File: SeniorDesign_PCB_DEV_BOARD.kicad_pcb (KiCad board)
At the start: 4 copper layers, 285.5 x 80.8 mm, 368 parts, among them J1 Conn_01x04_Pin, J10 Conn_01x02_Socket, J11 Conn_01x02_Pin, J12 USB_C_Receptacle_USB2.0_14P, J13 USB_C_Receptacle_USB2.0_14P, J14 IDC_Cable_02x08, J15 Conn_01x02_Pin, J16 Conn_01x04_Pin, J17 Conn_01x04_Pin, J18 Micro_SD_Card, J19 Conn_01x02_Socket, J2 Conn_01x02_Socket, J20 Conn_01x02_Socket, J21 MIC_I2S_CONNECTOR, J22 Conn_01x02_Socket, J23 Conn_01x02_Socket, J24 Conn_01x02_Socket, J3 Conn_01x03_Socket, J4 Conn_01x04_Pin, J5 Conn_01x02_Pin, J6 Conn_01x02_Socket, J7 Conn_01x02_Socket, J8 Conn_01x02_Socket, J9 Barrel_Jack, Q1 NMOS, Q2 NMOS, Q4 AO3400A, Q5 AO3400A, SW2 SW_Push, SW5 SW_Push, SW6 SW_Push, SW7 SW_Push, U1 TMP117xxDRV, U10 INA219AxD, U11 TLV62569ADRL, U12 USBLC6-2P6, U13 USBLC6-2P6, U14 ESP32-C3FH4, U15 TPS60400DBV, U16 TLV172IDCK, U2 RV-3028-C7, U3 STM32G474RETx, U5 MAX98357A, U6 TLV172IDCK, U7 TLV172IDCK, U8 MAX98357A, U9 INA219AxD, Y1 16MHz, Y2 40MHz

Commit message: taking a break
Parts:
- removed the AE1 at (236.9, 73.7)
- removed the C1 at (283.8, 90.4)
- removed the C10 at (293.2, 96.9)
- removed the C11 at (302.0, 96.3)
- removed the C12 at (250.1, 105.6)
- removed the C13 at (248.6, 105.6)
- removed the C14 at (301.7, 74.6)
- removed the C15 at (272.0, 75.3)
- removed the C16 at (255.2, 106.2)
- removed the C17 at (253.7, 106.2)
- removed the C18 at (317.2, 88.3)
- removed the C19 at (326.6, 91.1)
- removed the C2 at (283.9, 94.6)
- removed the C22 at (301.5, 107.5)
- removed the C23 at (240.6, 107.3)
- removed the C24 at (301.5, 105.7)
- removed the C25 at (240.6, 105.5)
- removed the C26 at (240.6, 87.3)
- removed the C27 at (240.6, 84.3)
- removed the C28 at (236.4, 74.7)
- removed the C29 at (236.4, 77.6)
- removed the C3 at (283.8, 92.5)
- removed the C30 at (236.4, 78.5)
- removed the C31 at (236.4, 81.5)
- removed the C32 at (236.7, 85.8)
- removed the C33 at (234.5, 83.1)
- removed the C34 at (236.7, 87.5)
- removed the C35 at (233.5, 85.6)
- removed the C36 at (229.5, 83.2)
- removed the C37 at (233.5, 88.0)
- removed the C38 at (227.9, 83.2)
- removed the C39 at (236.7, 89.2)
- removed the C4 at (283.9, 96.6)
- removed the C40 at (272.5, 86.3)
- removed the C41 at (253.7, 82.5)
- removed the C42 at (302.0, 86.3)
- removed the C43 at (284.3, 76.3)
- removed the C44 at (270.9, 79.5)
- removed the C45 at (229.6, 109.3)
- removed the C46 at (307.3, 77.1)
- removed the C47 at (281.7, 77.5)
- removed the C48 at (280.1, 77.5)
- removed the C49 at (281.7, 80.6)
- removed the C5 at (295.8, 88.8)
- removed the C50 at (280.1, 80.6)
- removed the C52 at (322.8, 69.8)
- removed the C53 at (275.1, 79.4)
- removed the C6 at (292.5, 86.6)
- removed the C7 at (286.1, 86.7)
- removed the C8 at (291.9, 83.8)
- removed the C9 at (288.8, 83.8)
- removed the D2 at (288.8, 103.8)
- removed the D4 at (322.5, 89.5)
- removed the D6 at (240.3, 102.3)
- removed the D7 at (301.3, 102.4)
- removed the D8 at (264.1, 73.6)
- removed the D9 at (234.4, 94.0)
- removed the F1 at (344.1, 77.4)
- removed the J1 at (310.1, 70.5)
- removed the J10 at (333.1, 104.1)
- removed J11: Conn_01x02_Pin, Connector_PinHeader_2.54mm:PinHeader_1x02_P2.54mm_Vertical
- removed the J12 at (298.3, 112.0)
- removed the J13 at (237.5, 111.8)
- removed the J14 at (286.1, 109.3)
- removed the J15 at (267.7, 70.5)
- removed the J16 at (221.1, 103.7)
- removed the J17 at (221.0, 83.7)
- removed the J18 at (254.5, 74.8)
- removed the J19 at (329.4, 111.4)
- removed the J2 at (285.0, 70.5)
- removed the J20 at (320.8, 111.4)
- removed the J21 at (337.5, 70.5)
- removed J22, J23: Conn_01x02_Socket, Connector_PinHeader_2.54mm:PinHeader_1x02_P2.54mm_Vertical
- removed J24: Conn_01x02_Socket, Connector_Phoenix_SPT:PhoenixContact_SPT_2.5_2-H-5.0_1x02_P5.0mm_Horizontal
- removed the J3 at (296.1, 70.5)
- removed the J4 at (307.1, 111.4)
- removed the J5 at (318.8, 70.5)
- removed the J6 at (276.3, 70.5)
- removed the J7 at (246.6, 111.4)
- removed the J8 at (256.0, 111.4)
- removed the L2 at (236.9, 76.1)
- removed the L3 at (236.8, 80.0)
- removed the L4 at (232.0, 82.4)
- removed the Q1 at (324.6, 100.9)
- removed the Q2 at (265.9, 76.6)
- removed the Q4 at (318.9, 104.8)
- removed the Q5 at (314.9, 104.9)
- removed the R10 at (291.1, 95.8)
- removed the R11 at (288.1, 101.6)
- removed the R12 at (273.0, 96.4)
- removed the R13 at (273.0, 93.6)
- removed the R14 at (273.0, 91.1)
- removed the R17 at (302.0, 89.9)
- removed the R18 at (299.1, 83.1)
- removed the R19 at (302.0, 93.1)
- removed the R2 at (298.9, 78.7)
- removed the R20 at (247.1, 102.5)
- removed the R21 at (274.5, 74.6)
- removed the R22 at (270.2, 76.7)
- removed the R23 at (267.6, 79.7)
- removed the R24 at (276.5, 77.2)
- removed the R25 at (277.2, 79.7)
- removed the R26 at (274.5, 82.9)
- removed the R27 at (270.2, 83.1)
- removed the R28 at (269.7, 85.8)
- removed the R29 at (270.5, 88.1)
- removed the R3 at (284.2, 74.6)
- removed the R30 at (255.0, 102.7)
- removed the R31 at (329.0, 96.0)
- removed the R32 at (329.0, 99.1)
- removed the R33 at (324.9, 83.4)
- removed the R34 at (258.0, 102.7)
- removed the R35 at (250.1, 102.5)
- removed the R36 at (292.6, 74.6)
- removed the R37 at (302.0, 83.0)
- removed the R38 at (325.0, 93.2)
- removed the R39 at (321.5, 93.2)
- removed the R45 at (240.0, 112.5)
- removed the R46 at (295.8, 112.7)
- removed the R47 at (234.9, 112.4)
- removed the R48 at (297.5, 106.7)
- removed the R49 at (299.1, 106.7)
- removed the R5 at (288.6, 98.2)
- removed the R50 at (236.7, 106.6)
- removed the R51 at (238.2, 106.6)
- removed the R52 at (268.7, 77.4)
- removed the R53 at (268.7, 73.8)
- removed the R54 at (234.4, 91.0)
- removed the R55 at (228.6, 84.3)
- removed the R56 at (228.6, 86.0)
- removed the R57 at (232.7, 80.8)
- removed the R58 at (231.5, 90.9)
- removed the R59 at (228.6, 88.0)
- removed the R6 at (291.8, 92.9)
- removed the R60 at (232.7, 79.2)
- removed the R61 at (298.1, 113.8)
- removed the R62 at (237.5, 113.7)
- removed the R68 at (315.5, 83.3)
- removed the R69 at (317.6, 80.0)
- removed the R7 at (307.3, 78.7)
- removed the R70 at (313.9, 83.3)
- removed the R71 at (314.5, 80.0)
- removed the R72 at (324.1, 82.0)
- removed the R73 at (324.1, 80.4)
- removed the R74 at (321.0, 80.4)
- removed the R75 at (321.0, 82.0)
- removed the R76 at (229.6, 112.4)
- removed the R78 at (230.4, 114.8)
- removed the R79 at (229.4, 97.1)
- removed the R8 at (307.4, 75.6)
- removed the R80 at (319.8, 101.3)
- removed the R81 at (317.9, 101.2)
- removed the R82 at (327.4, 112.3)
- removed the R83 at (315.8, 101.3)
- removed the R84 at (313.9, 101.3)
- removed the R85 at (318.6, 112.2)
- removed the R9 at (289.3, 95.8)
- removed the SW2 at (304.6, 92.2)
- removed the SW5 at (304.7, 81.5)
- removed the SW6 at (227.2, 114.0)
- removed the SW7 at (230.2, 99.5)
- removed the U1 at (298.9, 78.7)
- removed the U10 at (323.8, 86.5)
- removed the U12 at (298.3, 103.6)
- removed the U13 at (237.5, 103.4)
- removed the U14 at (235.0, 86.3)
- removed the U15 at (284.5, 78.9)
- removed the U16 at (275.1, 79.6)
- removed the U2 at (307.4, 77.6)
- removed the U3 at (288.8, 92.5)
- removed the U5 at (248.8, 105.6)
- removed the U6 at (270.9, 79.8)
- removed the U7 at (272.5, 86.6)
- removed the U8 at (256.7, 105.6)
- removed the U9 at (320.0, 84.7)
- removed the Y1 at (290.3, 80.6)
- removed the Y2 at (243.7, 85.8)
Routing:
- net 3V3: track 277.3 -> 136.7 mm, vias 73 -> 36
- net /ESP32C3/SPI1_MISO: track 235.1 -> 122.9 mm, vias 8 -> 4
- net 5V: track 206.0 -> 98.9 mm, vias 18 -> 12
- net /Power/I2C3_SCL: track 216.6 -> 110.0 mm, vias 7 -> 3
- net /ESP32C3/SPI1_MOSI: track 197.9 -> 98.2 mm, vias 8 -> 4
- net USB_5V: track 214.7 -> 115.4 mm, vias 13 -> 6
- net /ESP32C3/SPI1_SCLK: track 193.6 -> 102.0 mm, vias 8 -> 4
- net /Power/I2C3_SDA: track 172.4 -> 94.3 mm, vias 5 -> 2
- net /ESP32C3/SPI1_CS_ESP: track 177.2 -> 105.4 mm, vias 4 -> 2
- net /STM32G4/I2S3_CK: track 101.2 -> 43.7 mm, vias 2 -> 1
- net /STM32G4/I2S3_WS: track 97.8 -> 42.7 mm, vias 2 -> 1
- net /Analog/LEFT_SD_MODE: track 110.2 -> 55.1 mm, vias 4 -> 2
- net /STM32G4/I2S3_SD: track 95.3 -> 41.0 mm, vias 2 -> 1
- net /ESP32C3/ESP32_RST: track 101.3 -> 50.6 mm
- net /STM32G4/nRST: track 102.1 -> 52.5 mm
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- removed copper zone on B.Cu, net (none)
- removed copper zone on F.Cu, net /Power/5V_AMPS_1
- removed copper zone on F.Cu, net Net-(J10-Pin_1)
- removed copper zone on F.Cu, net Net-(J24-Pin_2)
- removed copper zone on B.Cu, net USB_5V
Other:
- board size 285.5 x 80.8 mm -> 98.3 x 80.8 mm
- board text removed: "MASHED PCB"
- board text removed: "TEAM 20"
- board text removed: "V1 Rev0"

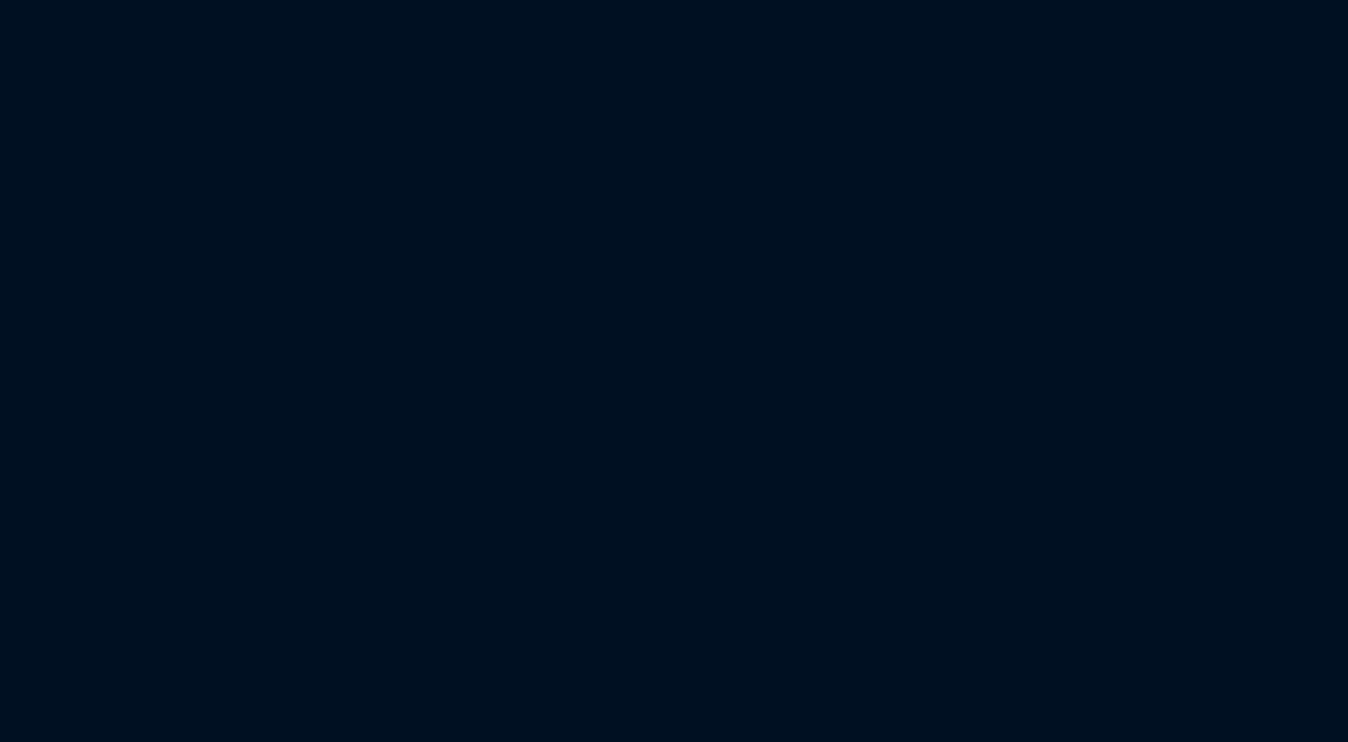
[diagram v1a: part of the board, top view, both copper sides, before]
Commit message: got rid of second buck
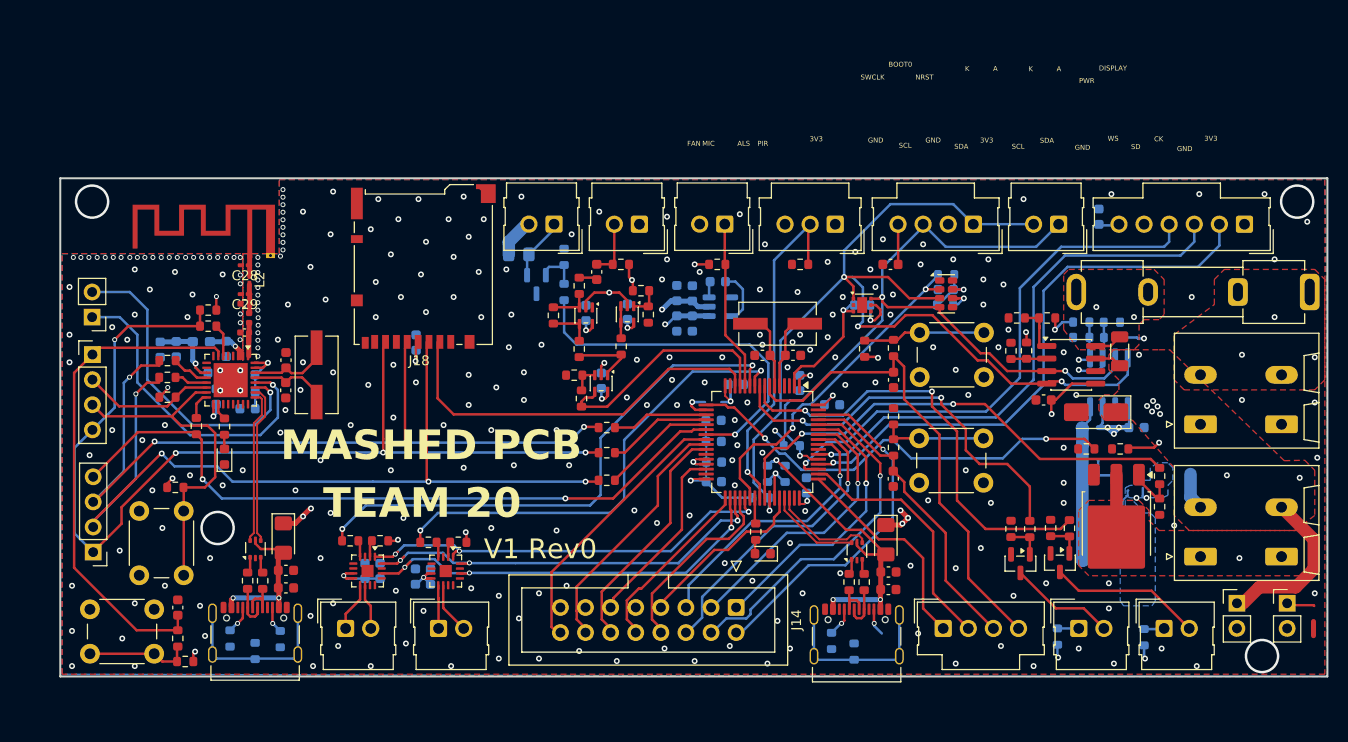
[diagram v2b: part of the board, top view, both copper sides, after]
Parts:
- added AE1: Antenna_Shield, RF_Antenna:Texas_SWRA117D_2.4GHz_Left, F.Cu at (236.9, 73.7)
- added C1: 1u, Capacitor_SMD:C_0603_1608Metric, B.Cu at (283.8, 90.4)
- added C10: 100n, Capacitor_SMD:C_0603_1608Metric, B.Cu at (293.2, 96.9)
- added C11: 100n, Capacitor_SMD:C_0603_1608Metric, F.Cu at (302.0, 96.3)
- added C12: 10u, Capacitor_SMD:C_0603_1608Metric, B.Cu at (250.1, 105.6)
- added C13: 100n, Capacitor_SMD:C_0603_1608Metric, B.Cu at (248.6, 105.6)
- added C14: 100n, Capacitor_SMD:C_0603_1608Metric, F.Cu at (301.7, 74.6)
- added C15: 1uF, Capacitor_SMD:C_0603_1608Metric, F.Cu at (272.0, 75.3)
- added C16: 10u, Capacitor_SMD:C_0603_1608Metric, B.Cu at (255.2, 106.2)
- added C17: 100n, Capacitor_SMD:C_0603_1608Metric, B.Cu at (253.7, 106.2)
- added C18: 100n, Capacitor_SMD:C_0603_1608Metric, F.Cu at (317.2, 88.3)
- added C19: 100n, Capacitor_SMD:C_0603_1608Metric, B.Cu at (326.6, 91.1)
- added C2: 100n, Capacitor_SMD:C_0603_1608Metric, B.Cu at (283.9, 94.6)
- added C22: 1u, Capacitor_SMD:C_0603_1608Metric, F.Cu at (301.5, 107.5)
- added C23: 1u, Capacitor_SMD:C_0603_1608Metric, F.Cu at (240.6, 107.3)
- added C24: 100n, Capacitor_SMD:C_0603_1608Metric, F.Cu at (301.5, 105.7)
- added C25: 100n, Capacitor_SMD:C_0603_1608Metric, F.Cu at (240.6, 105.5)
- added C26: 22p, Capacitor_SMD:C_0603_1608Metric, F.Cu at (240.6, 87.3)
- added C27: 22p, Capacitor_SMD:C_0603_1608Metric, F.Cu at (240.6, 84.3)
- added C28: DNP, Capacitor_SMD:C_0201_0603Metric_Pad0.64x0.40mm_HandSolder, F.Cu at (236.4, 74.7)
- added C29: DNP, Capacitor_SMD:C_0201_0603Metric_Pad0.64x0.40mm_HandSolder, F.Cu at (236.4, 77.6)
- added C3: 100n, Capacitor_SMD:C_0603_1608Metric, B.Cu at (283.8, 92.5)
- added C30: DNP, Capacitor_SMD:C_0402_1005Metric, F.Cu at (236.4, 78.5)
- added C31: DNP, Capacitor_SMD:C_0402_1005Metric, F.Cu at (236.4, 81.5)
- added C32: 100n, Capacitor_SMD:C_0603_1608Metric, B.Cu at (236.7, 85.8)
- added C33: 1u, Capacitor_SMD:C_0603_1608Metric, B.Cu at (234.5, 83.1)
- added C34: 100n, Capacitor_SMD:C_0603_1608Metric, B.Cu at (236.7, 87.5)
- added C35: 100n, Capacitor_SMD:C_0603_1608Metric, B.Cu at (233.5, 85.6)
- added C36: 100n, Capacitor_SMD:C_0603_1608Metric, B.Cu at (229.5, 83.2)
- added C37: 100n, Capacitor_SMD:C_0603_1608Metric, B.Cu at (233.5, 88.0)
- added C38: 10u, Capacitor_SMD:C_0603_1608Metric, B.Cu at (227.9, 83.2)
- added C39: 1u, Capacitor_SMD:C_0603_1608Metric, B.Cu at (236.7, 89.2)
- added C4: 100n, Capacitor_SMD:C_0603_1608Metric, B.Cu at (283.9, 96.6)
- added C40: 100n, Capacitor_SMD:C_0603_1608Metric, B.Cu at (272.5, 86.3)
- added C41: 100n, Capacitor_SMD:C_0603_1608Metric, B.Cu at (253.7, 82.5)
- added C42: 100n, Capacitor_SMD:C_0603_1608Metric, F.Cu at (302.0, 86.3)
- added C43: 1u, Capacitor_SMD:C_0603_1608Metric, B.Cu at (284.3, 76.3)
- added C44: 100n, Capacitor_SMD:C_0603_1608Metric, B.Cu at (270.9, 79.5)
- added C45: 100n, Capacitor_SMD:C_0603_1608Metric, F.Cu at (229.6, 109.3)
- added C46: 100n, Capacitor_SMD:C_0603_1608Metric, B.Cu at (307.3, 77.1)
- added C47: 100n, Capacitor_SMD:C_0603_1608Metric, B.Cu at (281.7, 77.5)
- added C48: 1u, Capacitor_SMD:C_0603_1608Metric, B.Cu at (280.1, 77.5)
- added C49: 1u, Capacitor_SMD:C_0603_1608Metric, B.Cu at (281.7, 80.6)
- added C5: 100n, Capacitor_SMD:C_0603_1608Metric, B.Cu at (295.8, 88.8)
- added C50: 100n, Capacitor_SMD:C_0603_1608Metric, B.Cu at (280.1, 80.6)
- added C52: 100n, Capacitor_SMD:C_0603_1608Metric, B.Cu at (322.8, 69.8)
- added C53: 100n, Capacitor_SMD:C_0603_1608Metric, B.Cu at (275.1, 79.4)
- added C6: 100n, Capacitor_SMD:C_0603_1608Metric, B.Cu at (292.5, 86.6)
- added C7: 100n, Capacitor_SMD:C_0603_1608Metric, B.Cu at (286.1, 86.7)
- added C8: 22p, Capacitor_SMD:C_0603_1608Metric, F.Cu at (291.9, 83.8)
- added C9: 22p, Capacitor_SMD:C_0603_1608Metric, F.Cu at (288.8, 83.8)
- added D2: LED, LED_SMD:LED_0603_1608Metric, F.Cu at (288.8, 103.8)
- added D4: SMAJ5.0A, Diode_SMD:D_SMA, F.Cu at (322.5, 89.5)
- added D6: D, Diode_SMD:D_1206_3216Metric_Pad1.42x1.75mm_HandSolder, F.Cu at (240.3, 102.3)
- added D7: D, Diode_SMD:D_1206_3216Metric_Pad1.42x1.75mm_HandSolder, F.Cu at (301.3, 102.4)
- added D8: D, Diode_SMD:D_0805_2012Metric_Pad1.15x1.40mm_HandSolder, B.Cu at (264.1, 73.6)
- added D9: LED, LED_SMD:LED_0603_1608Metric, F.Cu at (234.4, 94.0)
- added F1: RGEF1400, Fuse:Fuseholder_Clip-5x20mm_Keystone_3512P_Inline_P23.62x7.27mm_D1.02x2.41x1.02x1.57mm_Horizontal, F.Cu at (344.1, 77.4)
- added J1: Conn_01x04_Pin, Connector_Molex:Molex_SL_171971-0004_1x04_P2.54mm_Vertical, F.Cu at (310.1, 70.5)
- added J10: Conn_01x02_Socket, Connector_Phoenix_SPT:PhoenixContact_SPT_2.5_2-H-5.0_1x02_P5.0mm_Horizontal, F.Cu at (333.1, 104.1)
- added J11: Conn_01x02_Pin, Connector_PinHeader_2.54mm:PinHeader_1x02_P2.54mm_Vertical, F.Cu at (221.0, 79.9)
- added J12: USB_C_Receptacle_USB2.0_14P, Connector_USB:USB_C_Receptacle_Palconn_UTC16-G, F.Cu at (298.3, 112.0)
- added J13: USB_C_Receptacle_USB2.0_14P, Connector_USB:USB_C_Receptacle_Palconn_UTC16-G, F.Cu at (237.5, 111.8)
- added J14: IDC_Cable_02x08, Connector_IDC:IDC-Header_2x08_P2.54mm_Vertical, F.Cu at (286.1, 109.3)
- added J15: Conn_01x02_Pin, Connector_Molex:Molex_SL_171971-0002_1x02_P2.54mm_Vertical, F.Cu at (267.7, 70.5)
- added J16: Conn_01x04_Pin, Connector_PinHeader_2.54mm:PinHeader_1x04_P2.54mm_Vertical, F.Cu at (221.1, 103.7)
- added J17: Conn_01x04_Pin, Connector_PinHeader_2.54mm:PinHeader_1x04_P2.54mm_Vertical, F.Cu at (221.0, 83.7)
- added J18: Micro_SD_Card, Connector_Card:microSD_HC_Hirose_DM3BT-DSF-PEJS, F.Cu at (254.5, 74.8)
- added J19: Conn_01x02_Socket, Connector_Molex:Molex_SL_171971-0002_1x02_P2.54mm_Vertical, F.Cu at (329.4, 111.4)
- added J2: Conn_01x02_Socket, Connector_Molex:Molex_SL_171971-0002_1x02_P2.54mm_Vertical, F.Cu at (285.0, 70.5)
- added J20: Conn_01x02_Socket, Connector_Molex:Molex_SL_171971-0002_1x02_P2.54mm_Vertical, F.Cu at (320.8, 111.4)
- added J21: MIC_I2S_CONNECTOR, Connector_Molex:Molex_SL_171971-0006_1x06_P2.54mm_Vertical, F.Cu at (337.5, 70.5)
- added J22: Conn_01x02_Socket, Connector_PinHeader_2.54mm:PinHeader_1x02_P2.54mm_Vertical, F.Cu at (341.9, 108.9)
- added J23: Conn_01x02_Socket, Connector_PinHeader_2.54mm:PinHeader_1x02_P2.54mm_Vertical, F.Cu at (336.8, 108.9)
- added J24: Conn_01x02_Socket, Connector_Phoenix_SPT:PhoenixContact_SPT_2.5_2-H-5.0_1x02_P5.0mm_Horizontal, F.Cu at (333.1, 90.8)
- added J3: Conn_01x03_Socket, Connector_Molex:Molex_SL_171971-0003_1x03_P2.54mm_Vertical, F.Cu at (296.1, 70.5)
- added J4: Conn_01x04_Pin, Connector_Molex:Molex_SL_171971-0004_1x04_P2.54mm_Vertical, F.Cu at (307.1, 111.4)
- added J5: Conn_01x02_Pin, Connector_Molex:Molex_SL_171971-0002_1x02_P2.54mm_Vertical, F.Cu at (318.8, 70.5)
- added J6: Conn_01x02_Socket, Connector_Molex:Molex_SL_171971-0002_1x02_P2.54mm_Vertical, F.Cu at (276.3, 70.5)
- added J7: Conn_01x02_Socket, Connector_Molex:Molex_SL_171971-0002_1x02_P2.54mm_Vertical, F.Cu at (246.6, 111.4)
- added J8: Conn_01x02_Socket, Connector_Molex:Molex_SL_171971-0002_1x02_P2.54mm_Vertical, F.Cu at (256.0, 111.4)
- added L2: DNP, Inductor_SMD:L_0201_0603Metric_Pad0.64x0.40mm_HandSolder, F.Cu at (236.9, 76.1)
- added L3: DNP, Inductor_SMD:L_0402_1005Metric, F.Cu at (236.8, 80.0)
- added L4: 2n, Inductor_SMD:L_0603_1608Metric_Pad1.05x0.95mm_HandSolder, B.Cu at (232.0, 82.4)
- added Q1: NMOS, Package_TO_SOT_SMD:TO-252-3_TabPin2, F.Cu at (324.6, 100.9)
- added Q2: NMOS, Package_TO_SOT_SMD:SOT-23, B.Cu at (265.9, 76.6)
- added Q4: AO3400A, Package_TO_SOT_SMD:SOT-23, F.Cu at (318.9, 104.8)
- added Q5: AO3400A, Package_TO_SOT_SMD:SOT-23, F.Cu at (314.9, 104.9)
- added R10: 3.3k, Resistor_SMD:R_0603_1608Metric, B.Cu at (291.1, 95.8)
- added R11: 330, Resistor_SMD:R_0603_1608Metric, F.Cu at (288.1, 101.6)
- added R12: 0R, Resistor_SMD:R_0603_1608Metric, F.Cu at (273.0, 96.4)
- added R13: 0R, Resistor_SMD:R_0603_1608Metric, F.Cu at (273.0, 93.6)
- added R14: 0R, Resistor_SMD:R_0603_1608Metric, F.Cu at (273.0, 91.1)
- added R17: 10k, Resistor_SMD:R_0603_1608Metric, F.Cu at (302.0, 89.9)
- added R18: 10k, Resistor_SMD:R_0603_1608Metric, F.Cu at (299.1, 83.1)
- added R19: 1k, Resistor_SMD:R_0603_1608Metric, F.Cu at (302.0, 93.1)
- added R2: 10k, Resistor_SMD:R_0603_1608Metric, B.Cu at (298.9, 78.7)
- added R20: 0R, Resistor_SMD:R_0603_1608Metric, F.Cu at (247.1, 102.5)
- added R21: 2k2, Resistor_SMD:R_0603_1608Metric, F.Cu at (274.5, 74.6)
- added R22: 1k, Resistor_SMD:R_0603_1608Metric, F.Cu at (270.2, 76.7)
- added R23: 18k, Resistor_SMD:R_0603_1608Metric, F.Cu at (267.6, 79.7)
- added R24: 10k, Resistor_SMD:R_0603_1608Metric, F.Cu at (276.5, 77.2)
- added R25: 10k, Resistor_SMD:R_0603_1608Metric, F.Cu at (277.2, 79.7)
- added R26: 1k, Resistor_SMD:R_0603_1608Metric, F.Cu at (274.5, 82.9)
- added R27: 1k, Resistor_SMD:R_0603_1608Metric, F.Cu at (270.2, 83.1)
- added R28: 1k, Resistor_SMD:R_0603_1608Metric, F.Cu at (269.7, 85.8)
- added R29: 1k, Resistor_SMD:R_0603_1608Metric, F.Cu at (270.5, 88.1)
- added R3: 2k2, Resistor_SMD:R_0603_1608Metric, F.Cu at (284.2, 74.6)
- added R30: 210k, Resistor_SMD:R_0603_1608Metric, F.Cu at (255.0, 102.7)
- added R31: 10R, Resistor_SMD:R_0603_1608Metric, F.Cu at (329.0, 96.0)
- added R32: 10k, Resistor_SMD:R_0603_1608Metric, F.Cu at (329.0, 99.1)
- added R33: 2m, Resistor_SMD:R_1206_3216Metric, F.Cu at (324.9, 83.4)
- added R34: 0R, Resistor_SMD:R_0603_1608Metric, F.Cu at (258.0, 102.7)
- added R35: 0R, Resistor_SMD:R_0603_1608Metric, F.Cu at (250.1, 102.5)
- added R36: 100k, Resistor_SMD:R_0603_1608Metric, F.Cu at (292.6, 74.6)
- added R37: 1k, Resistor_SMD:R_0603_1608Metric, F.Cu at (302.0, 83.0)
- added R38: 10k, Resistor_SMD:R_0603_1608Metric, F.Cu at (325.0, 93.2)
- added R39: 10k, Resistor_SMD:R_0603_1608Metric, F.Cu at (321.5, 93.2)
- added R45: 5k1, Resistor_SMD:R_0603_1608Metric, B.Cu at (240.0, 112.5)
- added R46: 5k1, Resistor_SMD:R_0603_1608Metric, B.Cu at (295.8, 112.7)
- added R47: 5k1, Resistor_SMD:R_0603_1608Metric, B.Cu at (234.9, 112.4)
- added R48: 22R, Resistor_SMD:R_0603_1608Metric, F.Cu at (297.5, 106.7)
- added R49: 22R, Resistor_SMD:R_0603_1608Metric, F.Cu at (299.1, 106.7)
- added R5: 5k1, Resistor_SMD:R_0603_1608Metric, B.Cu at (288.6, 98.2)
- added R50: 22R, Resistor_SMD:R_0603_1608Metric, F.Cu at (236.7, 106.6)
- added R51: 22R, Resistor_SMD:R_0603_1608Metric, F.Cu at (238.2, 106.6)
- added R52: 10R, Resistor_SMD:R_0603_1608Metric, B.Cu at (268.7, 77.4)
- added R53: 10k, Resistor_SMD:R_0603_1608Metric, B.Cu at (268.7, 73.8)
- added R54: 330, Resistor_SMD:R_0603_1608Metric, F.Cu at (234.4, 91.0)
- added R55: 0R, Resistor_SMD:R_0603_1608Metric, F.Cu at (228.6, 84.3)
- added R56: 0R, Resistor_SMD:R_0603_1608Metric, F.Cu at (228.6, 86.0)
- added R57: 0R, Resistor_SMD:R_0603_1608Metric, F.Cu at (232.7, 80.8)
- added R58: 0R, Resistor_SMD:R_0603_1608Metric, F.Cu at (231.5, 90.9)
- added R59: 10k, Resistor_SMD:R_0603_1608Metric, F.Cu at (228.6, 88.0)
- added R6: 5k1, Resistor_SMD:R_0603_1608Metric, B.Cu at (291.8, 92.9)
- added R60: 10k, Resistor_SMD:R_0603_1608Metric, F.Cu at (232.7, 79.2)
- added R61: DNP, Resistor_SMD:R_0603_1608Metric, B.Cu at (298.1, 113.8)
- added R62: DNP, Resistor_SMD:R_0603_1608Metric, B.Cu at (237.5, 113.7)
- added R68: DNP, Resistor_SMD:R_0603_1608Metric, F.Cu at (315.5, 83.3)
- added R69: 0R, Resistor_SMD:R_0603_1608Metric, F.Cu at (317.6, 80.0)
- added R7: 10k, Resistor_SMD:R_0603_1608Metric, B.Cu at (307.3, 78.7)
- added R70: 0R, Resistor_SMD:R_0603_1608Metric, F.Cu at (313.9, 83.3)
- added R71: DNP, Resistor_SMD:R_0603_1608Metric, F.Cu at (314.5, 80.0)
- added R72: 0R, Resistor_SMD:R_0603_1608Metric, B.Cu at (324.1, 82.0)
- added R73: DNP, Resistor_SMD:R_0603_1608Metric, B.Cu at (324.1, 80.4)
- added R74: DNP, Resistor_SMD:R_0603_1608Metric, B.Cu at (321.0, 80.4)
- added R75: 0R, Resistor_SMD:R_0603_1608Metric, B.Cu at (321.0, 82.0)
- added R76: 1k, Resistor_SMD:R_0603_1608Metric, F.Cu at (229.6, 112.4)
- added R78: 10k, Resistor_SMD:R_0603_1608Metric, F.Cu at (230.4, 114.8)
- added R79: 10k, Resistor_SMD:R_0603_1608Metric, F.Cu at (229.4, 97.1)
- added R8: 10k, Resistor_SMD:R_0603_1608Metric, B.Cu at (307.4, 75.6)
- added R80: 10, Resistor_SMD:R_0603_1608Metric, F.Cu at (319.8, 101.3)
- added R81: 10k, Resistor_SMD:R_0603_1608Metric, F.Cu at (317.9, 101.2)
- added R82: 17, Resistor_SMD:R_0603_1608Metric, B.Cu at (327.4, 112.3)
- added R83: 10, Resistor_SMD:R_0603_1608Metric, F.Cu at (315.8, 101.3)
- added R84: 10k, Resistor_SMD:R_0603_1608Metric, F.Cu at (313.9, 101.3)
- added R85: 17, Resistor_SMD:R_0603_1608Metric, B.Cu at (318.6, 112.2)
- added R9: 17k, Resistor_SMD:R_0603_1608Metric, B.Cu at (289.3, 95.8)
- added SW2: SW_Push, Button_Switch_THT:SW_PUSH_6mm, F.Cu at (304.6, 92.2)
- added SW5: SW_Push, Button_Switch_THT:SW_PUSH_6mm, F.Cu at (304.7, 81.5)
- added SW6: SW_Push, Button_Switch_THT:SW_PUSH_6mm, F.Cu at (227.2, 114.0)
- added SW7: SW_Push, Button_Switch_THT:SW_PUSH_6mm, F.Cu at (230.2, 99.5)
- added U1: TMP117xxDRV, Package_SON:WSON-6-1EP_2x2mm_P0.65mm_EP1x1.6mm, F.Cu at (298.9, 78.7)
- added U10: INA219AxD, Package_SO:SOIC-8_3.9x4.9mm_P1.27mm, B.Cu at (323.8, 86.5)
- added U12: USBLC6-2P6, Package_TO_SOT_SMD:SOT-666, F.Cu at (298.3, 103.6)
- added U13: USBLC6-2P6, Package_TO_SOT_SMD:SOT-666, F.Cu at (237.5, 103.4)
- added U14: ESP32-C3FH4, Package_DFN_QFN:QFN-32-1EP_5x5mm_P0.5mm_EP3.45x3.45mm, F.Cu at (235.0, 86.3)
- added U15: TPS60400DBV, Package_TO_SOT_SMD:SOT-23-5, B.Cu at (284.5, 78.9)
- added U16: TLV172IDCK, Package_TO_SOT_SMD:SOT-353_SC-70-5, F.Cu at (275.1, 79.6)
- added U2: RV-3028-C7, Package_SON:MicroCrystal_C7_SON-8_1.5x3.2mm_P0.9mm, F.Cu at (307.4, 77.6)
- added U3: STM32G474RETx, Package_QFP:LQFP-64_10x10mm_P0.5mm, F.Cu at (288.8, 92.5)
- added U5: MAX98357A, Package_DFN_QFN:TQFN-16-1EP_3x3mm_P0.5mm_EP1.23x1.23mm, F.Cu at (248.8, 105.6)
- added U6: TLV172IDCK, Package_TO_SOT_SMD:SOT-353_SC-70-5, F.Cu at (270.9, 79.8)
- added U7: TLV172IDCK, Package_TO_SOT_SMD:SOT-353_SC-70-5, F.Cu at (272.5, 86.6)
- added U8: MAX98357A, Package_DFN_QFN:TQFN-16-1EP_3x3mm_P0.5mm_EP1.23x1.23mm, F.Cu at (256.7, 105.6)
- added U9: INA219AxD, Package_SO:SOIC-8_3.9x4.9mm_P1.27mm, F.Cu at (320.0, 84.7)
- added Y1: 16MHz, Crystal:Crystal_SMD_ECS_CSM3X-2Pin_7.6x4.1mm, F.Cu at (290.3, 80.6)
- added Y2: 40MHz, Crystal:Crystal_SMD_ECS_CSM3X-2Pin_7.6x4.1mm, F.Cu at (243.7, 85.8)
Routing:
- net 3V3: track 136.7 -> 277.3 mm, vias 36 -> 73
- net /ESP32C3/SPI1_MISO: track 122.9 -> 235.1 mm, vias 4 -> 8
- net 5V: track 98.9 -> 206.0 mm, vias 12 -> 18
- net /Power/I2C3_SCL: track 110.0 -> 216.6 mm, vias 3 -> 7
- net /ESP32C3/SPI1_MOSI: track 98.2 -> 197.9 mm, vias 4 -> 8
- net USB_5V: track 115.4 -> 214.7 mm, vias 6 -> 13
- net /ESP32C3/SPI1_SCLK: track 102.0 -> 193.6 mm, vias 4 -> 8
- net /Power/I2C3_SDA: track 94.3 -> 172.4 mm, vias 2 -> 5
- net /ESP32C3/SPI1_CS_ESP: track 105.4 -> 177.2 mm, vias 2 -> 4
- net /STM32G4/I2S3_CK: track 43.7 -> 101.2 mm, vias 1 -> 2
- net /STM32G4/I2S3_WS: track 42.7 -> 97.8 mm, vias 1 -> 2
- net /Analog/LEFT_SD_MODE: track 55.1 -> 110.2 mm, vias 2 -> 4
- net /STM32G4/I2S3_SD: track 41.0 -> 95.3 mm, vias 1 -> 2
- net /ESP32C3/ESP32_RST: track 50.6 -> 101.3 mm
- net /STM32G4/nRST: track 52.5 -> 102.1 mm
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- added copper zone on B.Cu, net (none)
- added copper zone on F.Cu, net /Power/5V_AMPS_1
- added copper zone on F.Cu, net Net-(J10-Pin_1)
- added copper zone on F.Cu, net Net-(J24-Pin_2)
- added copper zone on B.Cu, net USB_5V
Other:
- board size 98.3 x 80.8 mm -> 285.5 x 80.8 mm
- board text added: "MASHED PCB"
- board text added: "TEAM 20"
- board text added: "V1 Rev0"
